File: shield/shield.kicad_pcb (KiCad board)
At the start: 2 copper layers, 68.6 x 53.3 mm, 58 parts, among them U1 CD4051B

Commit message: Update via spacing
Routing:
- net Net-(A1-Pad14): track 135.4 -> 138.5 mm
- net Net-(A1-Pad13): track 136.6 -> 139.2 mm
- net Net-(A1-Pad12): track 137.9 -> 139.8 mm
- net Net-(A1-Pad11): track 135.4 -> 136.6 mm
- net Net-(A1-Pad10): track 136.0 -> 136.6 mm

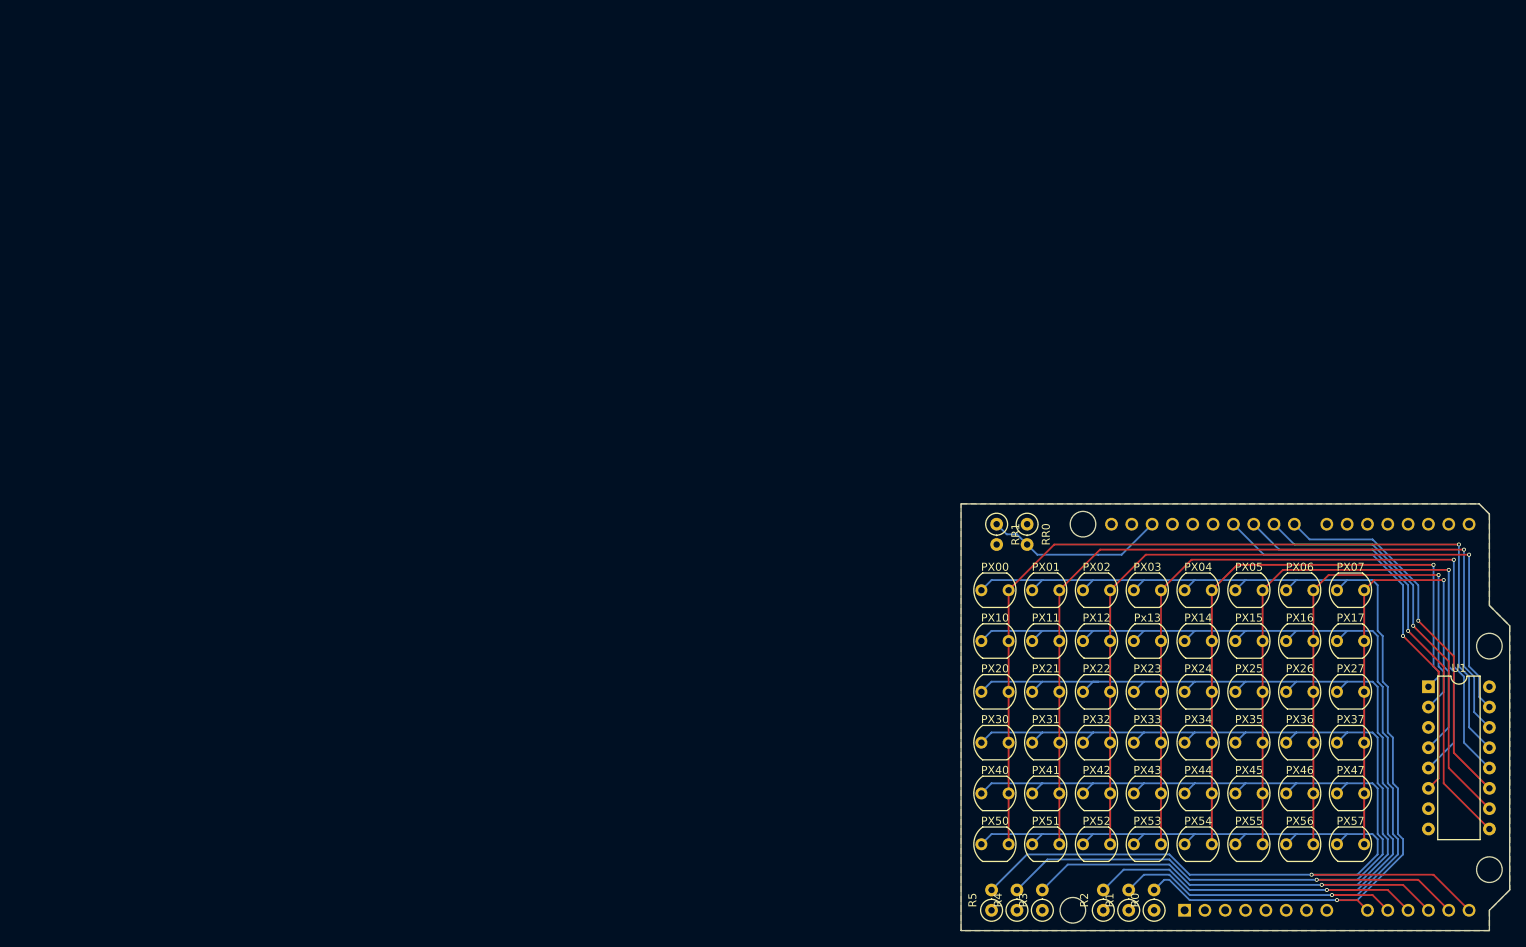
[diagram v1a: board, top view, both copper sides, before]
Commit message: Update shield to kicad 6
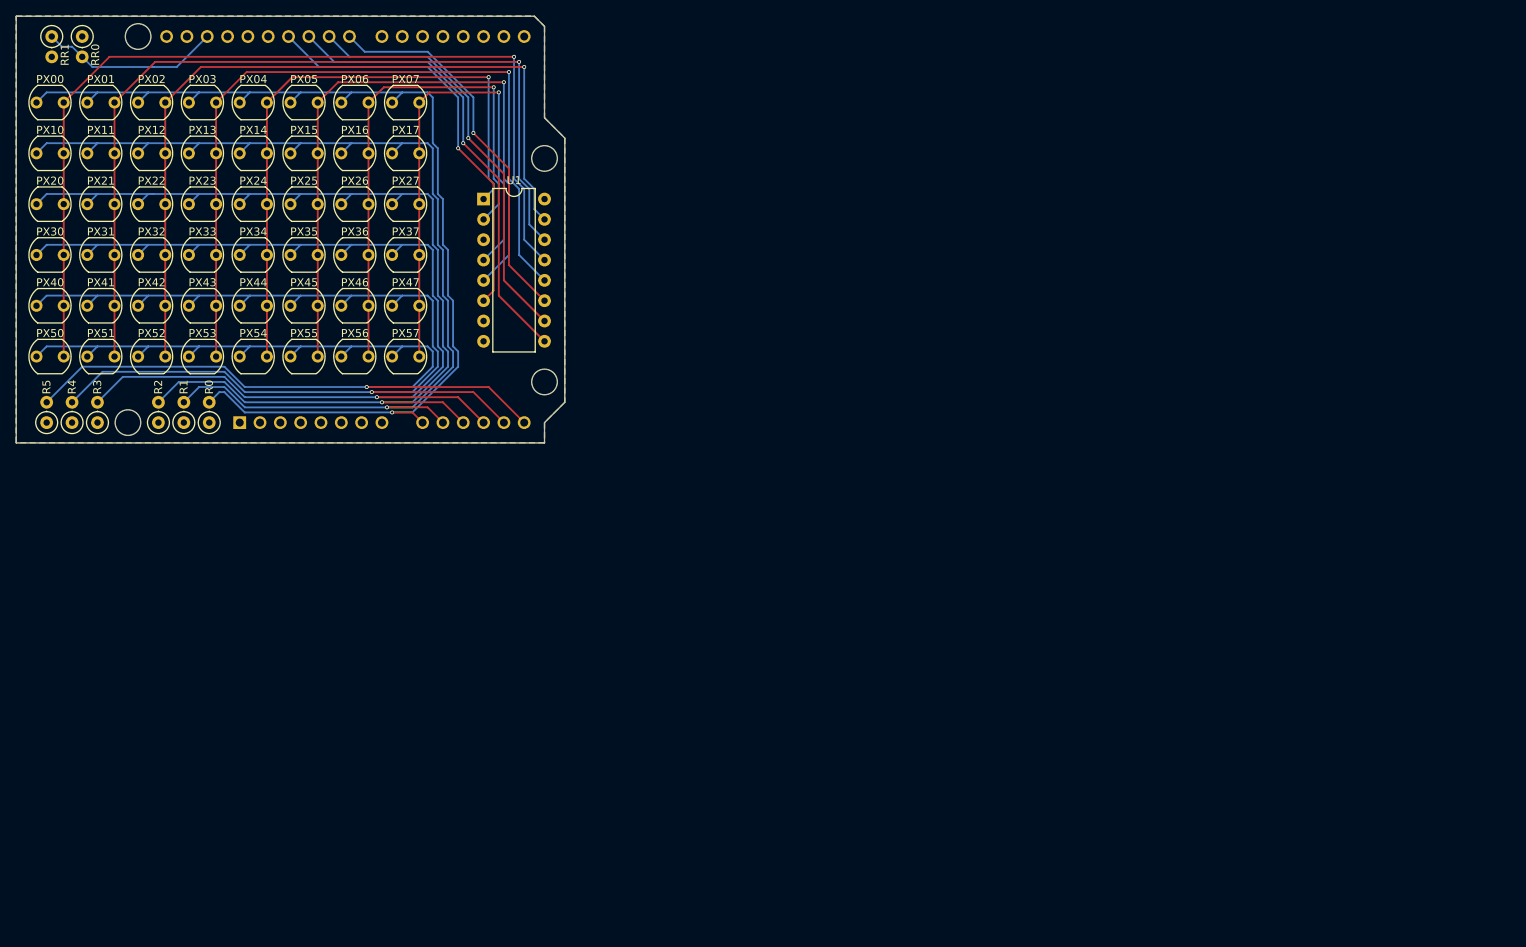
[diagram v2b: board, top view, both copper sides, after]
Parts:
- moved A1 132.9 mm to (99.1, 83.8)
- moved PX00 132.9 mm to (73.7, 43.8)
- moved PX01 132.9 mm to (80.0, 43.8)
- moved PX02 132.9 mm to (86.4, 43.8)
- moved PX03 132.9 mm to (92.7, 43.8)
- moved PX04 132.9 mm to (99.1, 43.8)
- moved PX05 132.9 mm to (105.4, 43.8)
- moved PX06 132.9 mm to (111.8, 43.8)
- moved PX07 132.9 mm to (118.1, 43.8)
- moved PX10 132.9 mm to (73.7, 50.2)
- moved PX11 132.9 mm to (80.0, 50.2)
- moved PX12 132.9 mm to (86.4, 50.2)
- moved PX13 132.9 mm to (92.7, 50.2)
- moved PX14 132.9 mm to (99.1, 50.2)
- moved PX15 132.9 mm to (105.4, 50.2)
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- renumbered Px13 to PX13
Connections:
- A1 pad 1: Net-(A1-Pad1) -> unconnected-(A1-Pad1)
- A1 pad 15: Net-(A1-Pad15) -> unconnected-(A1-Pad15)
- A1 pad 16: Net-(A1-Pad16) -> unconnected-(A1-Pad16)
- A1 pad 17: Net-(A1-Pad17) -> unconnected-(A1-Pad17)
- A1 pad 18: Net-(A1-Pad18) -> unconnected-(A1-Pad18)
- A1 pad 19: Net-(A1-Pad19) -> unconnected-(A1-Pad19)
- A1 pad 2: Net-(A1-Pad2) -> unconnected-(A1-Pad2)
- A1 pad 20: Net-(A1-Pad20) -> unconnected-(A1-Pad20)
- A1 pad 21: Net-(A1-Pad21) -> unconnected-(A1-Pad21)
- A1 pad 22: Net-(A1-Pad22) -> unconnected-(A1-Pad22)
- A1 pad 27: Net-(A1-Pad27) -> unconnected-(A1-Pad27)
- A1 pad 28: Net-(A1-Pad28) -> unconnected-(A1-Pad28)
- A1 pad 3: Net-(A1-Pad3) -> unconnected-(A1-Pad3)
- A1 pad 31: Net-(A1-Pad31) -> unconnected-(A1-Pad31)
- A1 pad 32: Net-(A1-Pad32) -> unconnected-(A1-Pad32)
- A1 pad 4: Net-(A1-Pad4) -> unconnected-(A1-Pad4)
- A1 pad 8: Net-(A1-Pad8) -> unconnected-(A1-Pad8)
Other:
- net class Default removed

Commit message: Update design rules
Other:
- board text added: "ὀπτικός"
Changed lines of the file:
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@@
     (34 "B.Paste" user)
     (35 "F.Paste" user)
-    (36 "B.SilkS" user "B.Silkscreen")
     (37 "F.SilkS" user "F.Silkscreen")
     (38 "B.Mask" user)
@@
       (layer "B.Mask" (type "Bottom Solder Mask") (thickness 0.01))
       (layer "B.Paste" (type "Bottom Solder Paste"))
-      (layer "B.SilkS" (type "Bottom Silk Screen"))
       (copper_finish "None")
       (dielectric_constraints no)
@@
   (gr_line (start 137.16 34.29) (end 137.16 45.72) (layer "Edge.Cuts") (width 0.05))
   (gr_line (start 135.89 33.02) (end 137.16 34.29) (layer "Edge.Cuts") (width 0.05))
+  (gr_text "ὀπτικός" (at 106.045 80.645) (layer "F.SilkS")
+    (effects (font (size 2.5 2.5) (thickness 0.5)))
+  )
   (segment (start 80.645 39.37) (end 88.265 39.37) (width 0.2286) (layer "B.Cu") (net 3))
   (segment (start 91.19 39.37) (end 88.265 39.37) (width 0.2286) (layer "B.Cu") (net 3))
@@
   (zone (net 30) (net_name "+5V") (layer "F.Cu") (hatch edge 0.508)
     (connect_pads yes (clearance 0.125))
-    (min_thickness 0.125)
+    (min_thickness 0.125) (filled_areas_thickness no)
     (fill yes (thermal_gap 0.508) (thermal_bridge_width 0.508))
     (polygon
@@
   (zone (net 29) (net_name "GND") (layer "B.Cu") (hatch edge 0.508)
     (connect_pads yes (clearance 0.125))
-    (min_thickness 0.125)
+    (min_thickness 0.125) (filled_areas_thickness no)
     (fill yes (thermal_gap 0.508) (thermal_bridge_width 0.508))
     (polygon
